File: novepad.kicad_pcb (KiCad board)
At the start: 4 copper layers, 99 x 59.5 mm, 143 parts, among them J101 NOVENA_LCD_CONN, J102 LP097QX1_CONN, J401 MOLEX_502250-8037, J402 MOLEX_502250-8037, U201 TPS61181, U202 TPS61181, U301 IT6251, U401 FT5816LPC, X301 27MHz 50ppm, 8-18pF, ESR < 80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, X401 12MHz 18pF

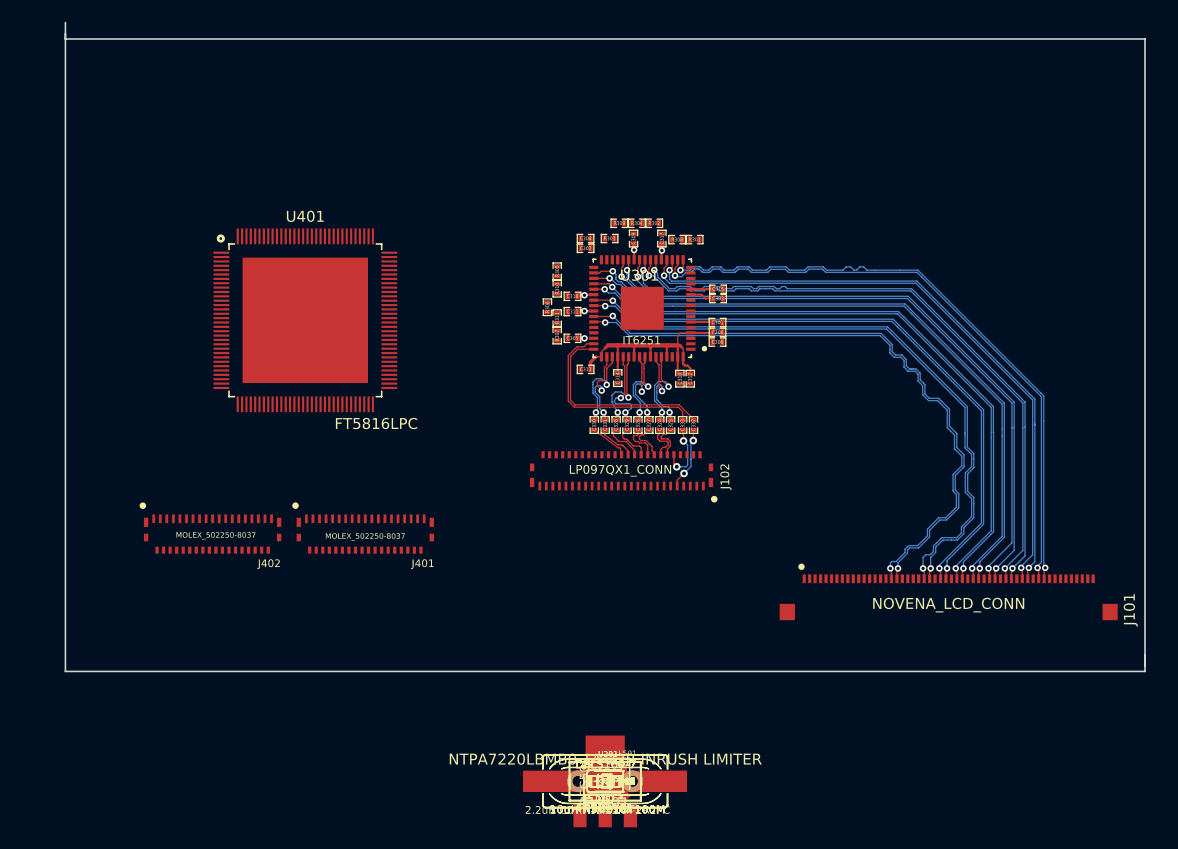
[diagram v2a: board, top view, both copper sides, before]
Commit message: Routed, passes DRC
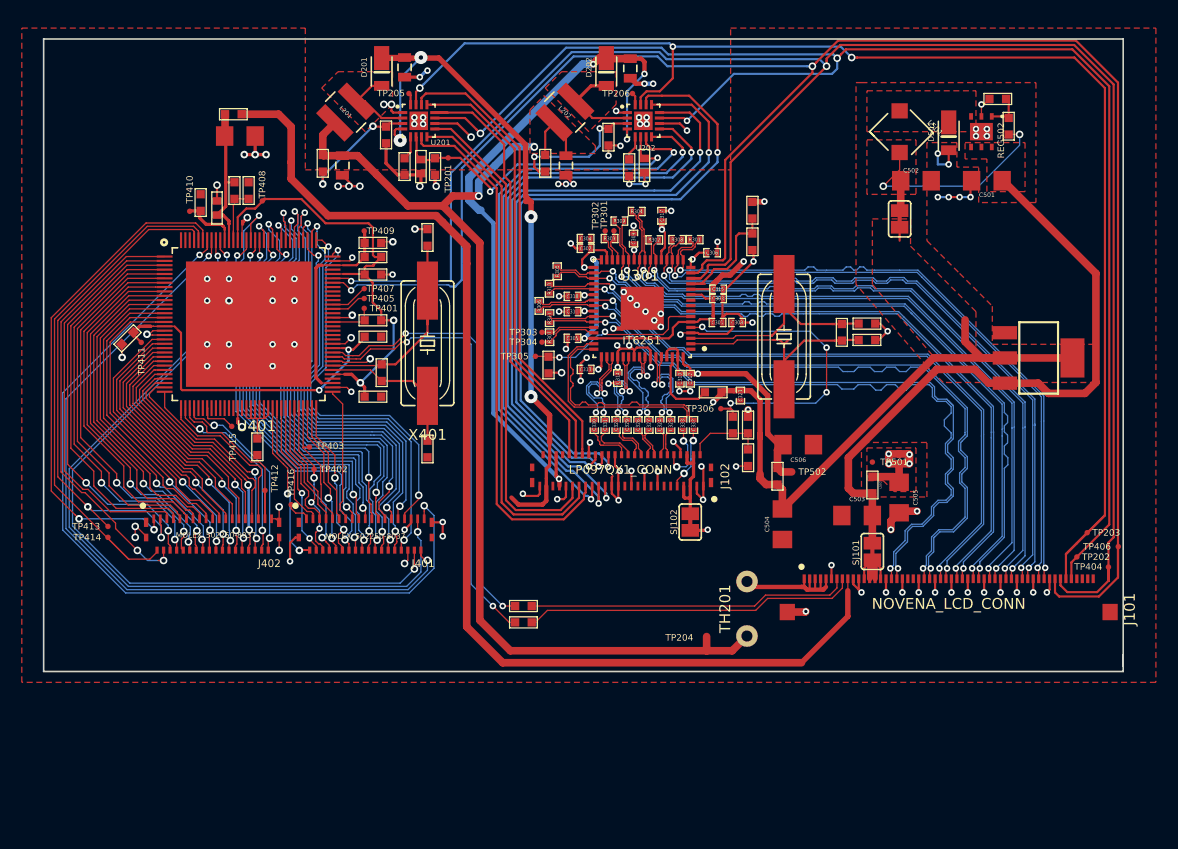
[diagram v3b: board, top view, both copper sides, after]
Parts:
- removed C319: 100nF 25V X5R, SMD_Packages:SMD-0402_c
- C201, C203, C207, C208: footprint FT:1206 -> FT:0805
- C202, C204, C403, C404, C406, C407, C409: footprint FT:1206 -> FT:0603
- C402: footprint SMD_Packages:SMD-0402_c -> FT:C0402
- R402: value 0R DNP -> 0R
- moved R501 72.2 mm to (173.5, 102.5), turned to 180 degrees
- moved R502 70.6 mm to (174.5, 105.0), turned to 270 degrees
- moved L401 70.0 mm to (103.4, 103.9), turned to 180 degrees
- moved REG502 68.8 mm to (172.0, 105.5), turned to 180 degrees
- moved D201 68.6 mm to (117.0, 99.6), turned to 270 degrees
- moved C207 68.0 mm to (119.1, 99.6), turned to 270 degrees
- moved C401 68.0 mm to (104.0, 105.9)
- moved D501 67.4 mm to (169.0, 105.5), turned to 270 degrees
- moved L201 65.8 mm to (113.7, 103.7), turned to 45 degrees
- moved TP205 65.6 mm to (119.5, 102.0), turned to 180 degrees
- moved D202 65.5 mm to (137.6, 99.6), turned to 270 degrees
- moved C208 65.4 mm to (139.8, 99.7), turned to 270 degrees
- moved L501 65.4 mm to (164.5, 105.5), turned to 315 degrees
- moved C501 65.3 mm to (172.5, 110.0), turned to 180 degrees
- moved C407 64.8 mm to (100.4, 112.0), turned to 90 degrees
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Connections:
- net Net-(C401-Pad1) renamed /Capacitive Touch (Optional)/VBUS
- net Net-(C502-Pad1) renamed /Power/18V_OUT
- net Net-(D201-PadA) renamed /Backlight Driver/SW_A
- net Net-(D202-PadA) renamed /Backlight Driver/SW_B
- net Net-(D501-PadK) renamed /Power/BUCK_SW
- net Net-(R402-Pad1) renamed /Capacitive Touch (Optional)/RX_UNUSED
- net Net-(R403-Pad1) renamed /Capacitive Touch (Optional)/D-
- net Net-(R404-Pad1) renamed /Capacitive Touch (Optional)/D+
- net Net-(R501-Pad1) renamed /Power/BUCK_FB
- net Net-(TP415-Pad1) renamed /Capacitive Touch (Optional)/TXUNUSED
- R405 pad 1: GND -> /Capacitive Touch (Optional)/PSEL
- R406 pad 1: GND -> /Capacitive Touch (Optional)/PSEL
- U201 pad 12: /Backlight Driver/CATHODE_4A -> /Backlight Driver/CATHODE_1A
- U201 pad 13: /Backlight Driver/CATHODE_5A -> /Backlight Driver/CATHODE_3A
- U201 pad 14: /Backlight Driver/CATHODE_6A -> /Backlight Driver/CATHODE_5A
- U201 pad 7: /Backlight Driver/CATHODE_1A -> /Backlight Driver/CATHODE_6A
- U201 pad 8: /Backlight Driver/CATHODE_2A -> /Backlight Driver/CATHODE_4A
- U201 pad 9: /Backlight Driver/CATHODE_3A -> /Backlight Driver/CATHODE_2A
- U202 pad 12: /Backlight Driver/CATHODE_4B -> /Backlight Driver/CATHODE_2B
- U202 pad 13: /Backlight Driver/CATHODE_5B -> /Backlight Driver/CATHODE_4B
- U202 pad 8: /Backlight Driver/CATHODE_2B -> /Backlight Driver/CATHODE_3B
- U202 pad 9: /Backlight Driver/CATHODE_3B -> /Backlight Driver/CATHODE_5B
- U401 pad 116: GND -> /Capacitive Touch (Optional)/PSEL
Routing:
- net GND: track 0.00 -> 247.4 mm, vias 0 -> 129
- net /Capacitive Touch (Optional)/I2C_SDA: track 0.00 -> 171.2 mm, vias 0 -> 2
- net /Capacitive Touch (Optional)/I2C_SCL: track 0.00 -> 169.0 mm, vias 0 -> 2
- net /Backlight Driver/BL_PWM: track 0.00 -> 133.8 mm, vias 0 -> 3
- net /Backlight Driver/BL_ENABLE: track 0.00 -> 126.7 mm, vias 0 -> 3
- net +1.8V: track 4.87 -> 120.0 mm, vias 1 -> 3
- net /Capacitive Touch (Optional)/USB_VBUS: track 0.00 -> 105.1 mm
- net /Backlight Driver/VBAT: track 0.00 -> 101.8 mm, vias 0 -> 2
- net /Capacitive Touch (Optional)/TX37: track 0.00 -> 76.8 mm, vias 0 -> 2
- net /Capacitive Touch (Optional)/TX39: track 0.00 -> 72.1 mm, vias 0 -> 2
- net /Capacitive Touch (Optional)/TX38: track 0.00 -> 70.4 mm, vias 0 -> 2
- net /Capacitive Touch (Optional)/TX40: track 0.00 -> 68.1 mm, vias 0 -> 2
- net /Backlight Driver/ANODE_A: track 0.00 -> 66.9 mm, vias 0 -> 4
- net /Backlight Driver/ANODE_B: track 0.00 -> 66.8 mm, vias 0 -> 4
- net /Backlight Driver/CATHODE_6B: track 0.00 -> 61.4 mm, vias 0 -> 2
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- added copper zone on F.Cu, net +1.8V
- added copper zone on VCC, net +1.8VA
- added copper zone on F.Cu, net +3.3V
- added copper zone on VCC, net +3.3V
- added copper zone on F.Cu, net +3.3VP
- added copper zone on F.Cu, net /Backlight Driver/SW_A
- added copper zone on F.Cu, net /Backlight Driver/SW_B
- added copper zone on F.Cu, net /Backlight Driver/VBAT
- added copper zone on F.Cu, net /Power/18V_OUT
- added copper zone on F.Cu, net /Power/BUCK_SW
- added copper zone on F.Cu, net GND
- added copper zone on GND, net GND
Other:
- board size 99 x 59.5 mm -> 99 x 58 mm
- net class LVDS_DP1/3 added: clearance 0.1, trace_width 0.1, via_dia 0.6, via_drill 0.3
- net class LVDS_LM3 removed
- net class eDP_ACC_DP0.1/2 added: clearance 0.1, trace_width 0.1, via_dia 0.6, via_drill 0.3
- net class eDP_ACC_LM0.2 removed
- net class eDP_AUX_DP0.2/3 added: clearance 0.1, trace_width 0.1, via_dia 0.6, via_drill 0.3
- net class eDP_AUX_LM0.5 removed
- net class eDP_AUX_OUT_DP0.2/2 added: clearance 0.2, trace_width 0.2, via_dia 0.7, via_drill 0.4
- net class eDP_AUX_OUT_LM0.5 removed
- net class eDP_DP0.2/2 added: clearance 0.1, trace_width 0.1, via_dia 0.6, via_drill 0.3
- net class eDP_LM0.5 removed
